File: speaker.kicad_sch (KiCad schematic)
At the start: 14 parts

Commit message: Correction in speaker address annotation
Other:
- note added: "IO = 0xDA"
- note removed: "IO = 0xD5"
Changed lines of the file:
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@@
     (effects (font (size 1.27 1.27)) (justify left bottom))
   )
-  (text "IO = 0xD5" (at 139.7 25.4 0)
+  (text "IO = 0xDA" (at 139.7 25.4 0)
     (effects (font (size 2.54 2.54)) (justify left bottom))
   )

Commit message: Some steps in bank switching and crtc circuits
- crtc pixel clock generator
- 2k ram, enabling logic (heavily incomplete)
- other 2k ram, annotation regarding data bus
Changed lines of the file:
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@@
+    (stroke (width 0) (type default) (color 0 0 0 0))
+  )
+  (wire (pts (xy 90.17 46.99) (xy 113.03 46.99))
     (stroke (width 0) (type default) (color 0 0 0 0))
   )
@@
   )
   (bus (pts (xy 57.15 82.55) (xy 57.15 90.17))
+    (stroke (width 0) (type default) (color 0 0 0 0))
+  )
+  (wire (pts (xy 90.17 49.53) (xy 113.03 49.53))
     (stroke (width 0) (type default) (color 0 0 0 0))
   )
@@
   )
   (wire (pts (xy 184.15 105.41) (xy 190.5 105.41))
+    (stroke (width 0) (type default) (color 0 0 0 0))
+  )
+  (wire (pts (xy 90.17 80.01) (xy 113.03 80.01))
     (stroke (width 0) (type default) (color 0 0 0 0))
   )
@@
     (stroke (width 0) (type default) (color 0 0 0 0))
   )
+  (wire (pts (xy 90.17 39.37) (xy 113.03 39.37))
+    (stroke (width 0) (type default) (color 0 0 0 0))
+  )

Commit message: Notes and minor fixes
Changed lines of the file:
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@@
+    (stroke (width 0) (type default))
+  )
+  (wire (pts (xy 34.29 49.53) (xy 64.77 49.53))
     (stroke (width 0) (type default))
   )

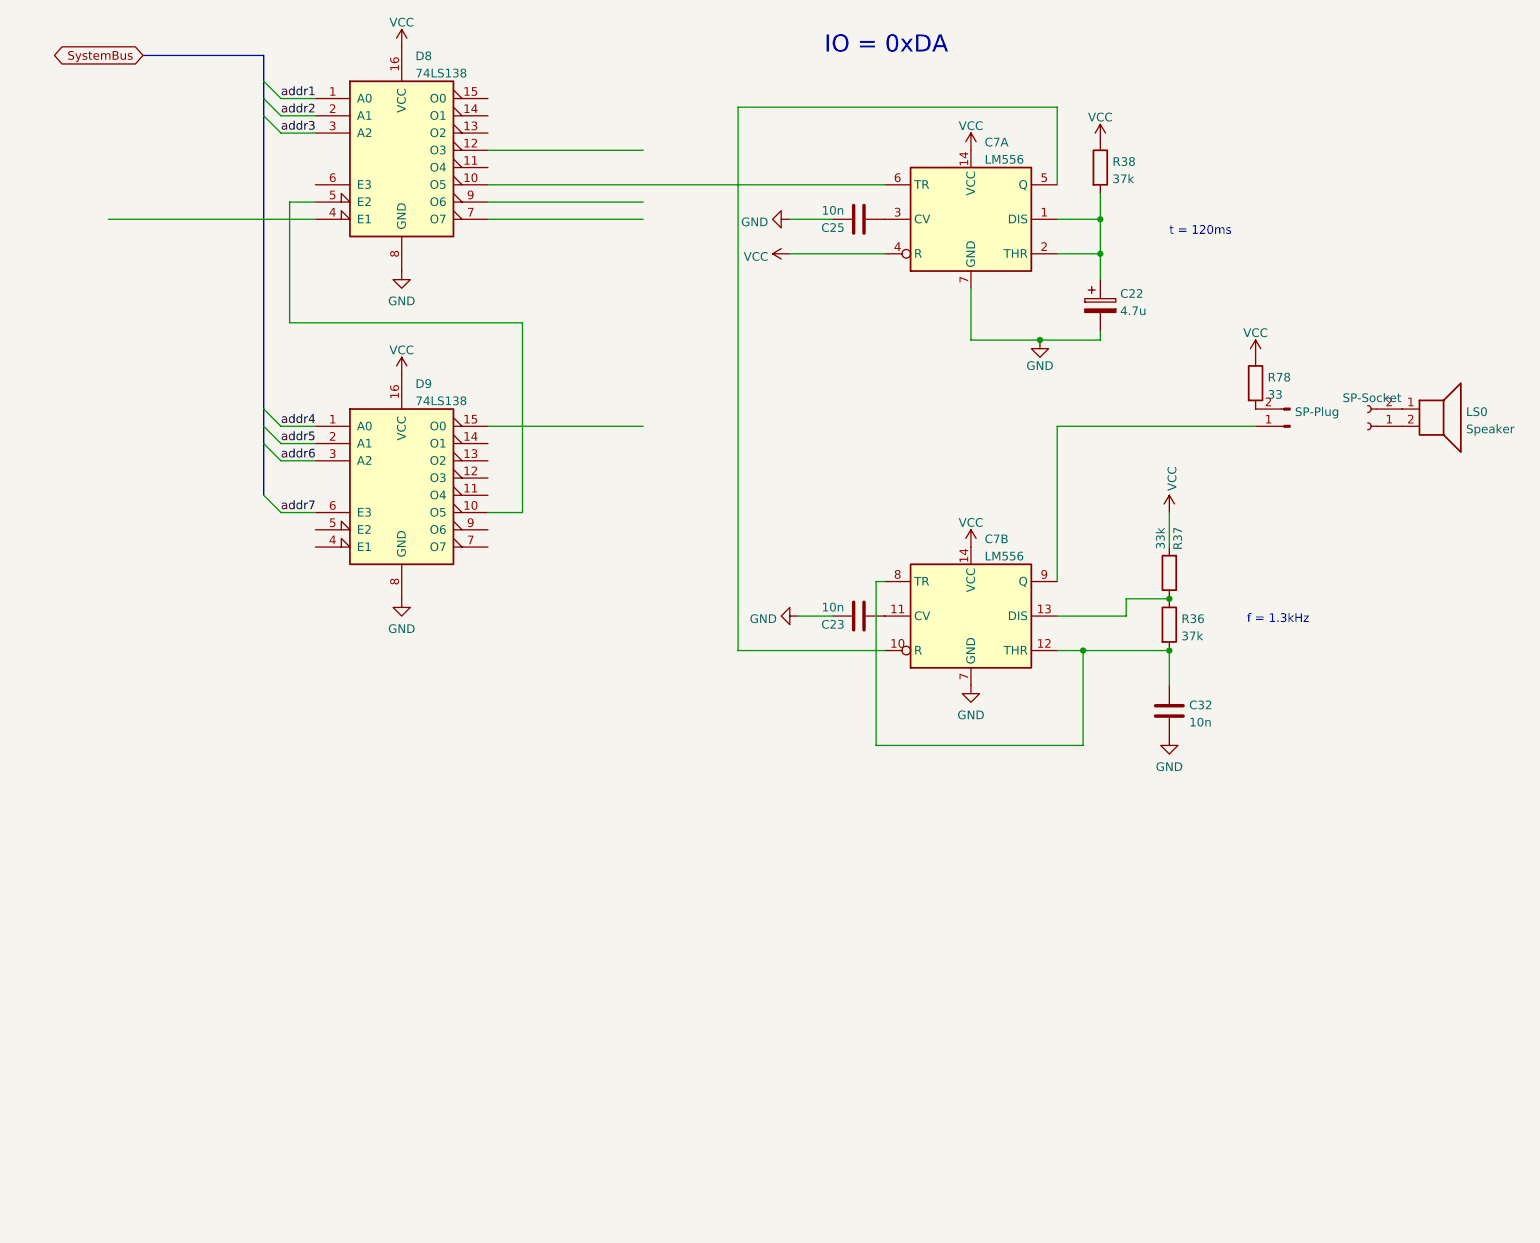
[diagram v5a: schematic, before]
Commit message: IO addressing space multiplexing and small IO description
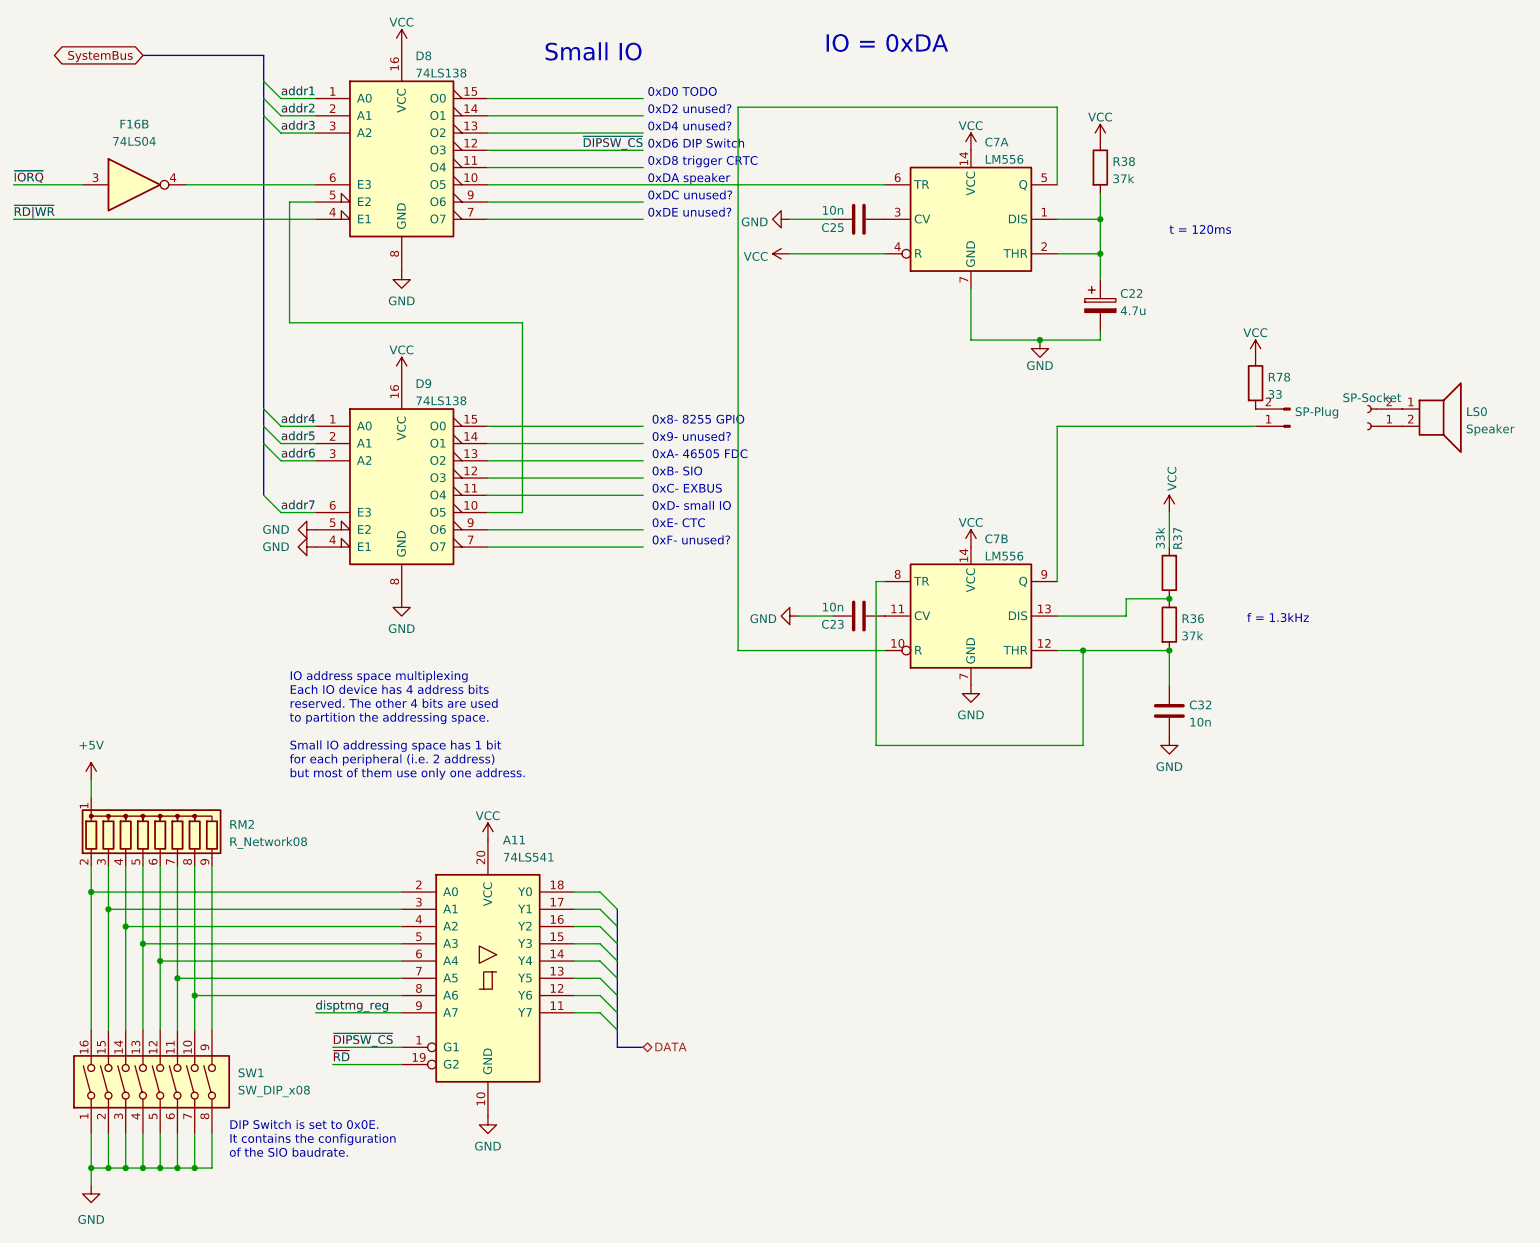
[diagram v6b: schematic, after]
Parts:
- added A11: 74LS541, symbol 74xx:74LS541
- added F16: 74LS04, symbol 74xx:74LS04
- added RM2: R_Network08, Resistor_THT:R_Array_SIP9, symbol Device:R_Network08
- added SW1: SW_DIP_x08, symbol Switch:SW_DIP_x08
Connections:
- net GND: now also D9.4 (E1), D9.5 (E2), A11.10 (GND), SW1.1, SW1.2, SW1.3, SW1.4, SW1.5, SW1.6, SW1.7, SW1.8
- net VCC: now also A11.20 (VCC)
- net ~{DIPSW_CS}: now reaches D8.12 (O3)
- net ~{DIPSW_CS}: now also A11.1 (G1)
- net ~{RD|WR}: now reaches D8.4 (E1)
- net at D8.6 (E3): now also F16.4
- new net: A11.2 (A0), RM2.2 (R1), SW1.16
- new net: A11.3 (A1), RM2.3 (R2), SW1.15
- new net: A11.4 (A2), RM2.4 (R3), SW1.14
- new net: A11.5 (A3), RM2.5 (R4), SW1.13
- new net: A11.6 (A4), RM2.6 (R5), SW1.12
- new net: A11.7 (A5), RM2.7 (R6), SW1.11
- new net: A11.8 (A6), RM2.8 (R7), SW1.10
- new net: RM2.9 (R8), SW1.9
- new net +5V: RM2.1 (common)
- new net disptmg_reg: A11.9 (A7)
- new net ~{IORQ}: F16.3
- new net ~{RD}: A11.19 (G2)
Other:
- note added: "0x8- 8255 GPIO"
- note added: "0x9- unused?"
- note added: "0xA- 46505 FDC"
- note added: "0xB- SIO"
- note added: "0xC- EXBUS"
- note added: "0xD- small IO"
- note added: "0xD0 TODO"
- note added: "0xD2 unused?"
- note added: "0xD4 unused?"
- note added: "0xD6 DIP Switch"
- note added: "0xD8 trigger CRTC"
- note added: "0xDA speaker"
- note added: "0xDC unused?"
- note added: "0xDE unused?"
- note added: "0xE- CTC"
- note added: "0xF- unused?"
- note added: "DIP Switch is set to 0x0E. It contains the configuration of the SIO baudrate."
- note added: "IO address space multiplexing Each IO device has 4 address bits reserved. The other 4 bits are used to partition the addressing space. Small IO addressing space has 1 bit for each peripheral (i.e. 2 address) but most of them use only one address."
- note added: "Small IO"

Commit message: Serial communication interface
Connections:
- net ~{SIO_CS}: now reaches D9.12 (O3)
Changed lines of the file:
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@@
     (effects (font (size 1.27 1.27)) (justify left bottom))
+  )
+  (label "~{SIO_CS}" (at 113.03 87.63 180) (fields_autoplaced)
+    (effects (font (size 1.27 1.27)) (justify right bottom))
   )
   (label "disptmg_reg" (at 64.77 166.37 0) (fields_autoplaced)

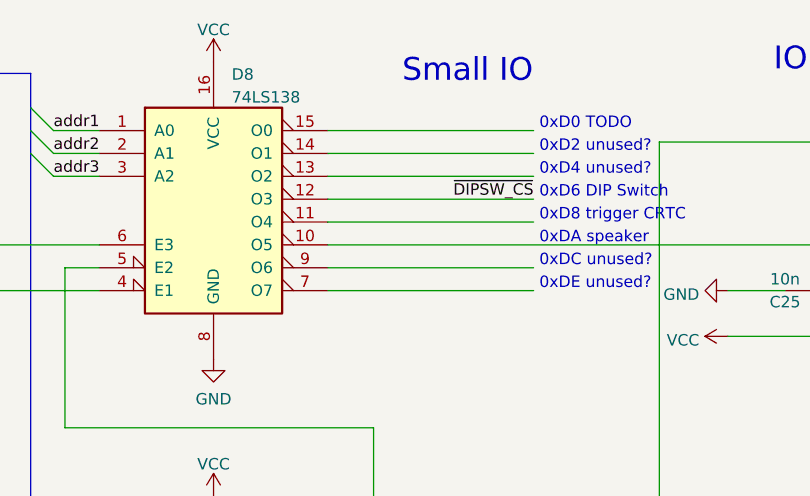
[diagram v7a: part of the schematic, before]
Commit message: Added FDC sheet (WIP), added partial parallel port inout
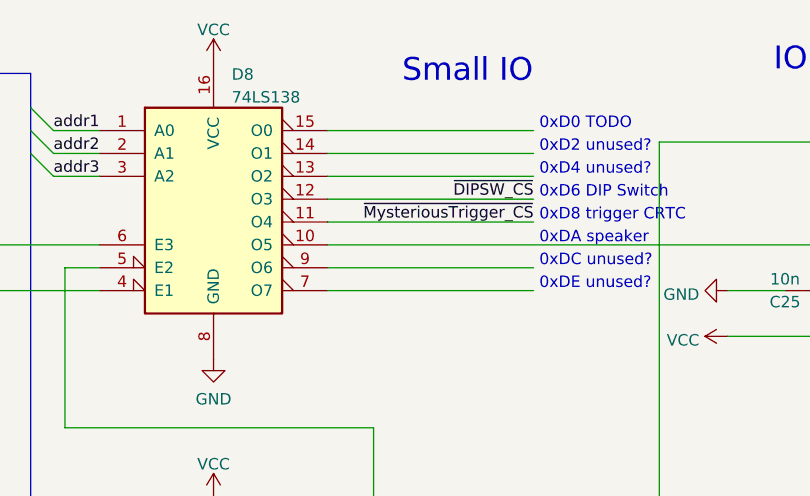
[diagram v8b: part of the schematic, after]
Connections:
- net ~{MysteriousTrigger_CS}: now reaches D8.11 (O4)
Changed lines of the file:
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@@
     (effects (font (size 1.27 1.27)) (justify left bottom))
+  )
+  (label "~{MysteriousTrigger_CS}" (at 113.03 41.91 180) (fields_autoplaced)
+    (effects (font (size 1.27 1.27)) (justify right bottom))
   )
   (label "addr7" (at 59.69 92.71 0) (fields_autoplaced)
